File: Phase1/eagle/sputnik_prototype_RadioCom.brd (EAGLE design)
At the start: 100 x 100 mm, 82 parts, among them X2 332-22, Y1 32MHz

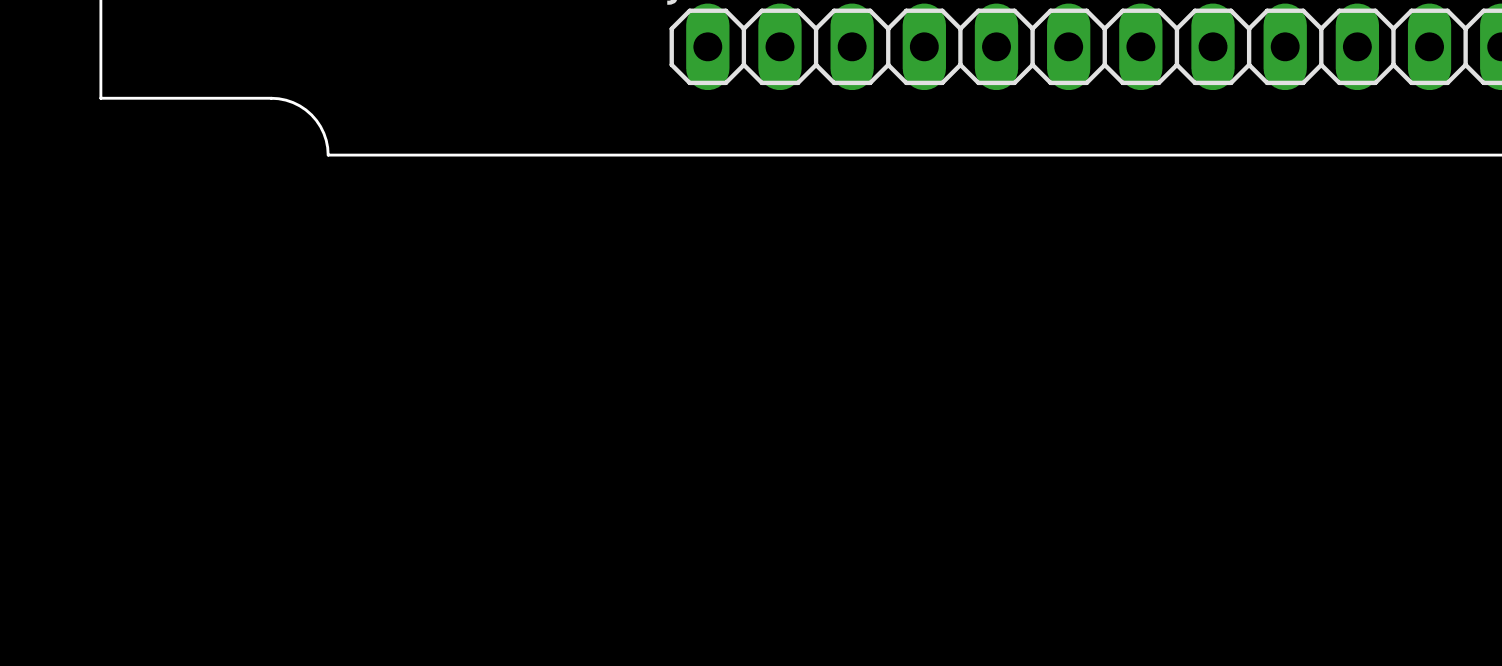
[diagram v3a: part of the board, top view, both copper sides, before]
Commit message: Added 44pin symbol and pull-up lines on SPI Cache
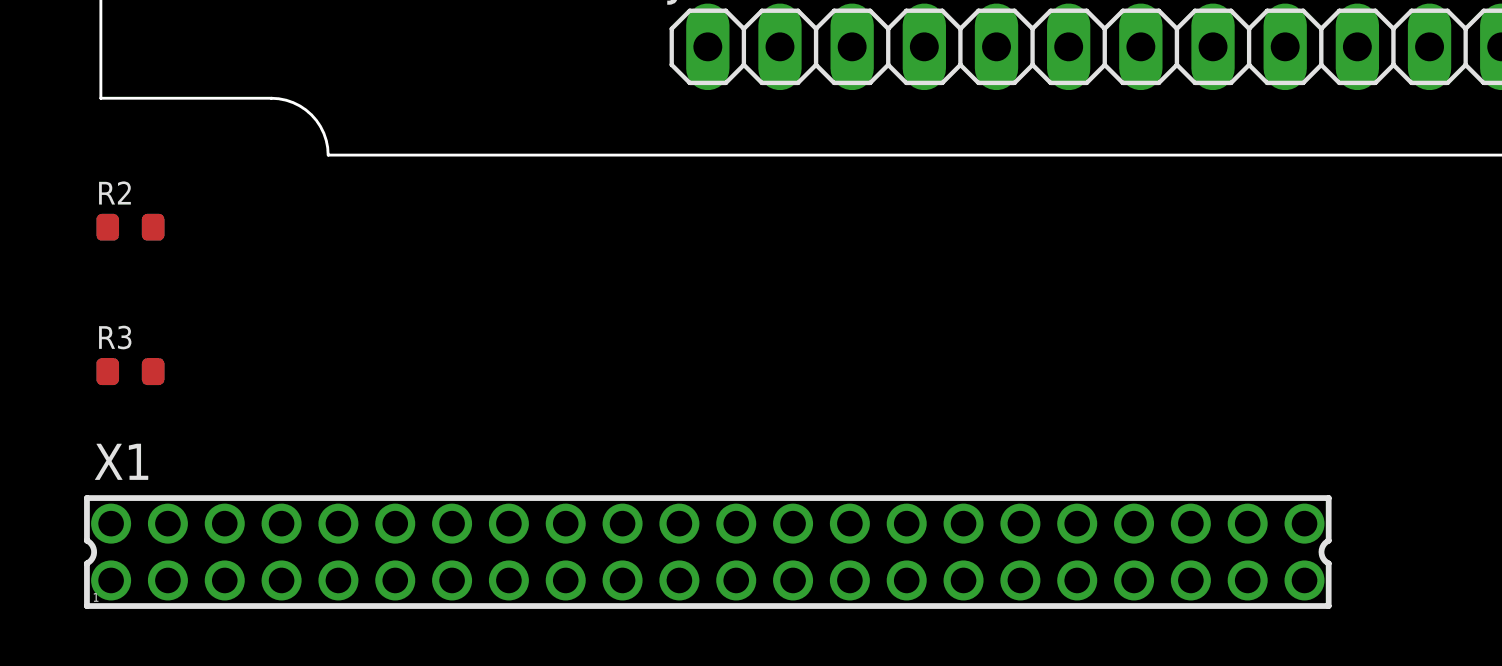
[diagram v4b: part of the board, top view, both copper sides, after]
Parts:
- added R2, R3: 200, rcl_custom:.0603-B-NOSILK
- added X1: 332-44, con-garry:332-44
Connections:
- new net N$11: R3.1, U$1.3
- net !HOLD: now also R2.1
- net !WP: no longer TP5.TP, U$1.3
- net 3.3V: now also R2.2, R3.2, TP5.TP
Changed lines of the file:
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@@
 <?xml version="1.0" encoding="utf-8"?>
 <!DOCTYPE eagle SYSTEM "eagle.dtd">
-<eagle version="7.3.0">
+<eagle version="7.4.0">
 <drawing>
 <settings>
@@
 <layer number="99" name="SpiceOrder" color="7" fill="1" visible="no" active="no"/>
 <layer number="100" name="TODO" color="12" fill="1" visible="yes" active="yes"/>
+<layer number="101" name="Hidden" color="7" fill="1" visible="yes" active="yes"/>
+<layer number="102" name="Changes" color="7" fill="1" visible="yes" active="yes"/>
+<layer number="103" name="tMap" color="7" fill="1" visible="yes" active="yes"/>
+<layer number="104" name="Name" color="7" fill="1" visible="yes" active="yes"/>
+<layer number="105" name="Beschreib" color="7" fill="1" visible="yes" active="yes"/>
+<layer number="106" name="BGA-Top" color="7" fill="1" visible="yes" active="yes"/>
+<layer number="107" name="BD-Top" color="7" fill="1" visible="yes" active="yes"/>
+<layer number="108" name="tplace-old" color="7" fill="1" visible="yes" active="yes"/>
+<layer number="109" name="ref-old" color="7" fill="1" visible="yes" active="yes"/>
+<layer number="110" name="fp0" color="7" fill="1" visible="yes" active="yes"/>
+<layer number="111" name="LPC17xx" color="7" fill="1" visible="yes" active="yes"/>
+<layer number="112" name="tSilk" color="7" fill="1" visible="yes" active="yes"/>
+<layer number="113" name="ReferenceLS" color="7" fill="1" visible="yes" active="yes"/>
+<layer number="116" name="Patch_BOT" color="7" fill="1" visible="yes" active="yes"/>
+<layer number="118" name="Rect_Pads" color="7" fill="1" visible="yes" active="yes"/>
+<layer number="121" name="_tsilk" color="7" fill="1" visible="yes" active="yes"/>
+<layer number="122" name="_bsilk" color="7" fill="1" visible="yes" active="yes"/>
+<layer number="123" name="tTestmark" color="7" fill="1" visible="yes" active="yes"/>
+<layer number="124" name="bTestmark" color="7" fill="1" visible="yes" active="yes"/>
+<layer number="125" name="_tNames" color="7" fill="1" visible="yes" active="yes"/>
+<layer number="126" name="_bNames" color="7" fill="1" visible="yes" active="yes"/>
+<layer number="127" name="_tValues" color="7" fill="1" visible="yes" active="yes"/>
+<layer number="128" name="_bValues" color="7" fill="1" visible="yes" active="yes"/>
+<layer number="131" name="tAdjust" color="7" fill="1" visible="yes" active="yes"/>
+<layer number="132" name="bAdjust" color="7" fill="1" visible="yes" active="yes"/>
+<layer number="144" name="Drill_legend" color="7" fill="1" visible="yes" active="yes"/>
+<layer number="150" name="Notes" color="7" fill="1" visible="yes" active="yes"/>
+<layer number="151" name="HeatSink" color="7" fill="1" visible="yes" active="yes"/>
+<layer number="152" name="_bDocu" color="7" fill="1" visible="yes" active="yes"/>
+<layer number="153" name="FabDoc1" color="7" fill="1" visible="yes" active="yes"/>
+<layer number="154" name="FabDoc2" color="7" fill="1" visible="yes" active="yes"/>
+<layer number="155" name="FabDoc3" color="7" fill="1" visible="yes" active="yes"/>
+<layer number="199" name="Contour" color="7" fill="1" visible="yes" active="yes"/>
+<layer number="200" name="200bmp" color="7" fill="1" visible="yes" active="yes"/>
+<layer number="201" name="201bmp" color="7" fill="1" visible="yes" active="yes"/>
+<layer number="202" name="202bmp" color="7" fill="1" visible="yes" active="yes"/>
+<layer number="203" name="203bmp" color="7" fill="1" visible="yes" active="yes"/>
+<layer number="204" name="204bmp" color="7" fill="1" visible="yes" active="yes"/>
+<layer number="205" name="205bmp" color="7" fill="1" visible="yes" active="yes"/>
+<layer number="206" name="206bmp" color="7" fill="1" visible="yes" active="yes"/>
+<layer number="207" name="207bmp" color="7" fill="1" visible="yes" active="yes"/>
+<layer number="208" name="208bmp" color="7" fill="1" visible="yes" active="yes"/>
+<layer number="209" name="209bmp" color="7" fill="1" visible="yes" active="yes"/>
+<layer number="210" name="210bmp" color="7" fill="1" visible="yes" active="yes"/>
+<layer number="211" name="211bmp" color="7" fill="1" visible="yes" active="yes"/>
+<layer number="212" name="212bmp" color="7" fill="1" visible="yes" active="yes"/>
+<layer number="213" name="213bmp" color="7" fill="1" visible="yes" active="yes"/>
+<layer number="214" name="214bmp" color="7" fill="1" visible="yes" active="yes"/>
+<layer number="215" name="215bmp" color="7" fill="1" visible="yes" active="yes"/>
+<layer number="216" name="216bmp" color="7" fill="1" visible="yes" active="yes"/>
+<layer number="217" name="217bmp" color="7" fill="1" visible="yes" active="yes"/>
+<layer number="218" name="218bmp" color="7" fill="1" visible="yes" active="yes"/>
+<layer number="219" name="219bmp" color="7" fill="1" visible="yes" active="yes"/>
+<layer number="220" name="220bmp" color="7" fill="1" visible="yes" active="yes"/>
+<layer number="221" name="221bmp" color="7" fill="1" visible="yes" active="yes"/>
+<layer number="222" name="222bmp" color="7" fill="1" visible="yes" active="yes"/>
+<layer number="223" name="223bmp" color="7" fill="1" visible="yes" active="yes"/>
+<layer number="224" name="224bmp" color="7" fill="1" visible="yes" active="yes"/>
+<layer number="231" name="Eagle3D_PG1" color="7" fill="1" visible="yes" active="yes"/>
+<layer number="232" name="Eagle3D_PG2" color="7" fill="1" visible="yes" active="yes"/>
+<layer number="233" name="Eagle3D_PG3" color="7" fill="1" visible="yes" active="yes"/>
+<layer number="248" name="Housing" color="7" fill="1" visible="yes" active="yes"/>
+<layer number="249" name="Edge" color="7" fill="1" visible="yes" active="yes"/>
+<layer number="250" name="Descript" color="7" fill="1" visible="yes" active="yes"/>
+<layer number="251" name="SMDround" color="7" fill="1" visible="yes" active="yes"/>
+<layer number="254" name="cooling" color="7" fill="1" visible="yes" active="yes"/>
 </layers>
 <board>
@@
 <attribute name="TP_SIGNAL_NAME" value="" x="3.81" y="11.43" size="1.778" layer="27" display="off"/>
 </element>
+<element name="R2" library="rcl_custom" package=".0603-B-NOSILK" value="200" x="2.54" y="-2.54"/>
+<element name="R3" library="rcl_custom" package=".0603-B-NOSILK" value="200" x="2.54" y="-7.62"/>
+<element name="X1" library="con-garry" package="332-44" value="332-44" x="22.86" y="-13.97"/>
 </elements>
 <signals>
@@
 <contactref element="C42" pad="2"/>
 <contactref element="JP2" pad="2"/>
+<contactref element="R2" pad="2"/>
+<contactref element="TP5" pad="TP"/>
+<contactref element="R3" pad="2"/>
 <wire x1="77.94" y1="57.15" x2="83.02" y2="57.15" width="0" layer="19" extent="1-1"/>
 <wire x1="74.46" y1="57.15" x2="77.94" y2="57.15" width="0" layer="19" extent="1-1"/>
@@
 <wire x1="64.3" y1="57.15" x2="69.38" y2="57.15" width="0" layer="19" extent="1-1"/>
 <wire x1="59.22" y1="57.15" x2="64.3" y2="57.15" width="0" layer="19" extent="1-1"/>
-<wire x1="41.41" y1="64.77" x2="59.22" y2="57.15" width="0" layer="19" extent="1-1"/>
+<wire x1="53.34" y1="71.12" x2="59.22" y2="57.15" width="0" layer="19" extent="1-1"/>
+<wire x1="41.41" y1="64.77" x2="53.34" y2="71.12" width="0" layer="19" extent="1-1"/>
 <wire x1="31.585" y1="47.58" x2="41.41" y2="64.77" width="0" layer="19" extent="1-1"/>
 <wire x1="34.2222" y1="40.08" x2="31.585" y2="47.58" width="0" layer="19" extent="1-1"/>
@@
 <wire x1="10.755" y1="32.35" x2="34.2222" y2="33.58" width="0" layer="19" extent="1-1"/>
 <wire x1="4.61" y1="57.15" x2="10.755" y2="32.35" width="0" layer="19" extent="1-1"/>
-<wire x1="25.4" y1="3.81" x2="4.61" y2="57.15" width="0" layer="19" extent="1-1"/>
-<wire x1="62.23" y1="3.175" x2="41.41" y2="64.77" width="0" layer="19" extent="1-1"/>
+<wire x1="25.4" y1="3.81" x2="34.85" y2="32.9522" width="0" layer="19" extent="1-1"/>
+<wire x1="3.34" y1="-2.54" x2="25.4" y2="3.81" width="0" layer="19" extent="1-1"/>
+<wire x1="3.34" y1="-7.62" x2="3.34" y2="-2.54" width="0" layer="19" extent="1-1"/>
+<wire x1="62.23" y1="3.175" x2="25.4" y2="3.81" width="0" layer="19" extent="1-1"/>
 </signal>
 <signal name="N$7">
@@
 <contactref element="KW0X" pad="32"/>
 <contactref element="TP10" pad="TP"/>
+<contactref element="R2" pad="1"/>
 <wire x1="12.025" y1="32.35" x2="39.85" y2="40.7078" width="0" layer="19" extent="1-1"/>
 <wire x1="3.81" y1="46.99" x2="12.025" y2="32.35" width="0" layer="19" extent="1-1"/>
+<wire x1="1.74" y1="-2.54" x2="12.025" y2="32.35" width="0" layer="19" extent="1-1"/>
 </signal>
 <signal name="!CS">
@@
 </signal>
 <signal name="!WP">
-<contactref element="U$1" pad="3"/>
 <contactref element="KW0X" pad="34"/>
-<contactref element="TP5" pad="TP"/>
-<wire x1="38.85" y1="40.7078" x2="53.34" y2="71.12" width="0" layer="19" extent="1-1"/>
-<wire x1="13.295" y1="27.15" x2="38.85" y2="40.7078" width="0" layer="19" extent="1-1"/>
 </signal>
 <signal name="PTC7">
@@
 <wire x1="3.81" y1="11.43" x2="34.2222" y2="36.58" width="0" layer="19" extent="1-1"/>
 </signal>
+<signal name="N$11">
+<contactref element="U$1" pad="3"/>
+<contactref element="R3" pad="1"/>
+<wire x1="1.74" y1="-7.62" x2="13.295" y2="27.15" width="0" layer="19" extent="1-1"/>
+</signal>
 </signals>

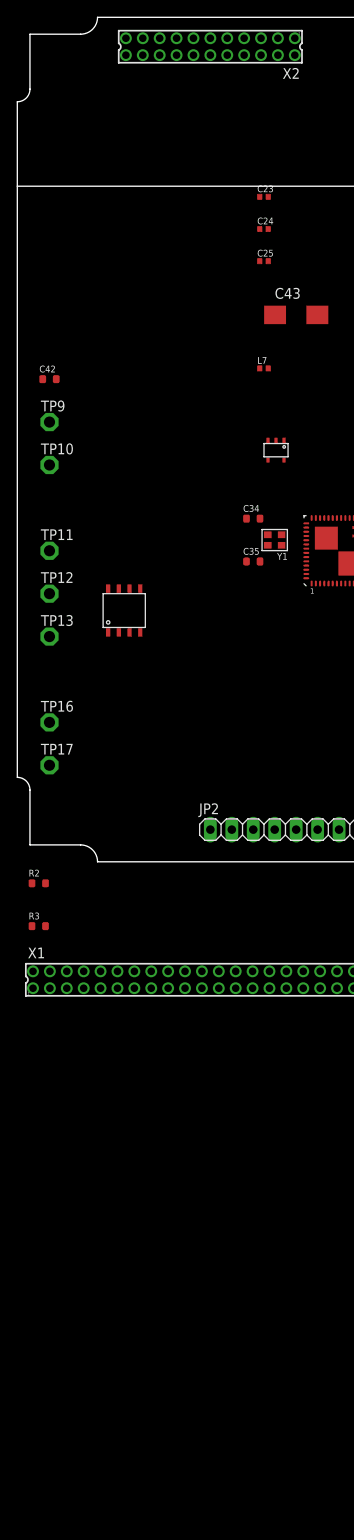
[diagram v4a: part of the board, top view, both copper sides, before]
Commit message: Fixed 22x2pinout, added PWR LEDs, fixed some NC issues
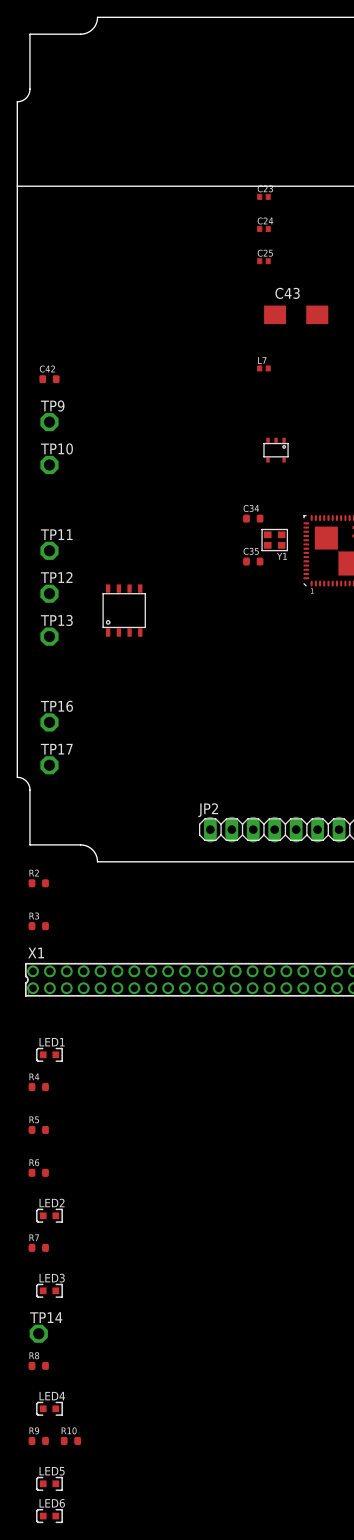
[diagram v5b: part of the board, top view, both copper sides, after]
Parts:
- removed X2: 332-22, con-garry:332-22
- added LED1, LED2, LED3, LED4, LED5, LED6: (no value), psas_c3_team05:LED-0603
- added R10, R4, R6, R7, R8, R9: 1k, rcl_custom:.0603-B-NOSILK
- added R5: 10k, rcl_custom:.0603-B-NOSILK
- added TP14: TPSPAD1-13, testpad:P1-13
- R2, R3: value 200 -> 10k
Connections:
- new net 3.3V1: LED2.A
- new net N$12: R5.1, TP14.TP, U$8.3
- new net N$14: LED1.K, R4.2
- new net N$15: LED2.K, R6.2
- new net N$20: LED3.K, R7.2
- new net N$22: LED4.K, R8.2
- new net N$26: LED5.K, R9.2
- new net N$28: LED5.A
- new net N$29: LED6.K, R10.2
- new net N$32: LED6.A
- net 3.3V: now also LED4.A
- net GND: now also LNA.1, R10.1, R4.1, R6.1, R7.1, R8.1, R9.1, X1.21, X1.22; no longer X2.21, X2.22
- net PTB17: now also X1.4; no longer X2.4
- net PTB2: now also X1.3; no longer X2.3
- net PTC1: now also X1.5; no longer X2.5
- net PTC2: now also X1.6; no longer X2.6
- net PTC3: now also X1.7; no longer X2.7
- net PTC4: now also X1.8; no longer X2.8
- net PTC5: now also X1.9; no longer X2.9
- net PTC6: now also X1.10; no longer X2.10
- net PTC7: now also X1.11; no longer X2.11
- net PTD0: now also X1.12; no longer X2.12
- net PTE16: now also X1.13; no longer X2.13
- net PTE17: now also X1.14; no longer X2.14
- net PTE18: now also X1.15; no longer X2.15
- net PTE19: now also X1.16; no longer X2.16
- net UART0_RX: now also X1.19, X1.20; no longer X2.19, X2.20
- net UART0_TX: now also X1.17, X1.18; no longer X2.17, X2.18
- net V+: now also LED1.A, R5.2, X1.1, X1.2; no longer X2.1, X2.2
- net VBIAS: no longer LNA.1
- net VPA: now also LED3.A
